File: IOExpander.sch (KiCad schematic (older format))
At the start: 6 parts, among them U11 MCP23017_SO

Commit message: start placement
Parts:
- renumbered C18 to C45, R12 to R75, R13 to R76, R14 to R77, R15 to R78, U11 to U7

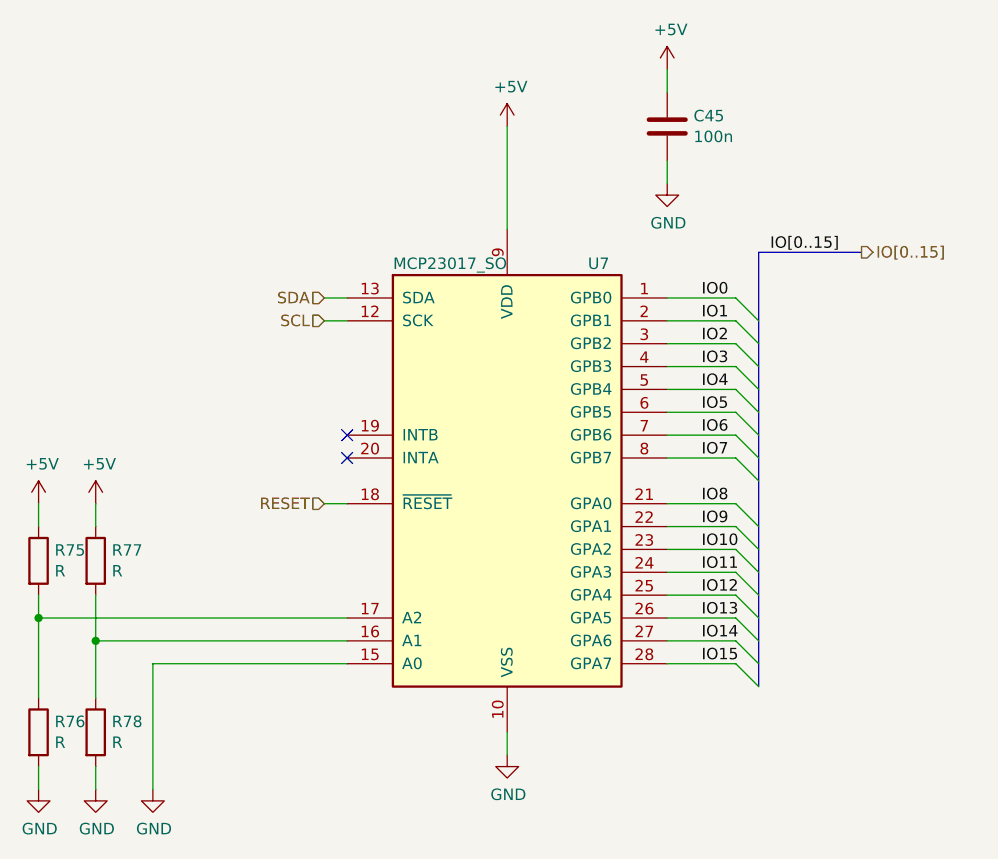
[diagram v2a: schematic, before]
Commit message: add TLE5602
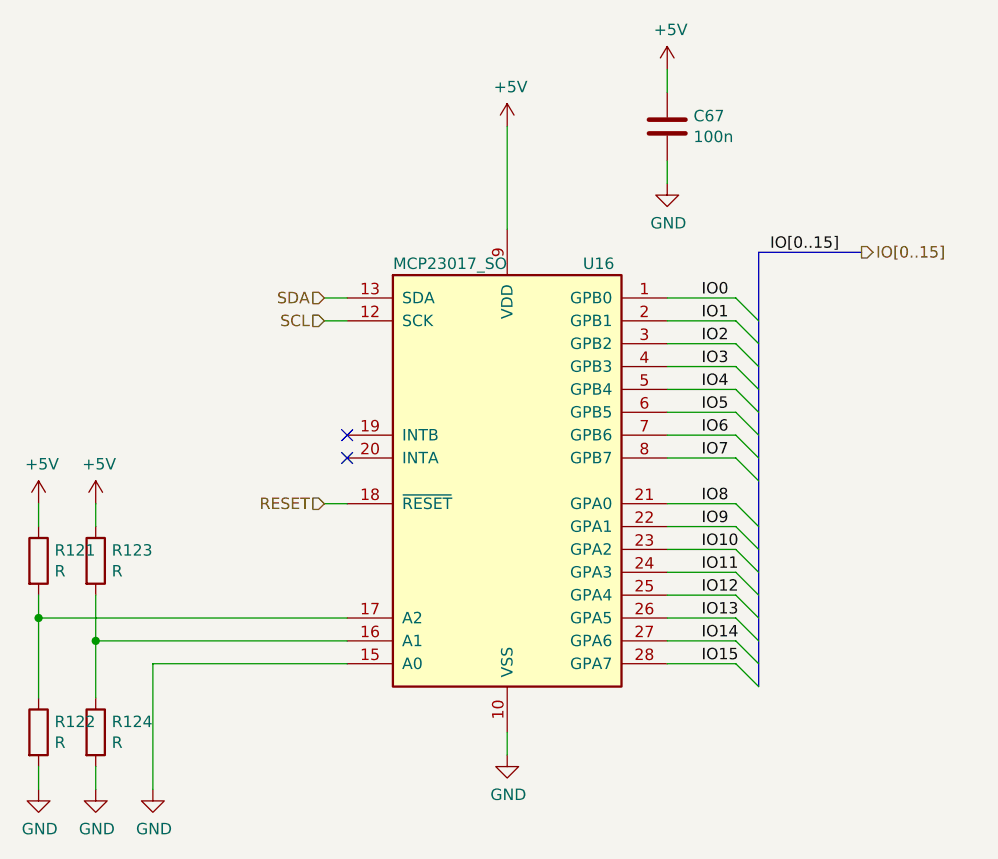
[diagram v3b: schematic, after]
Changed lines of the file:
@@
 $Descr A4 11693 8268
 encoding utf-8
-Sheet 8 22
+Sheet 13 22
 Title ""
 Date ""
@@
 AR Path="/60ADDFFD/60729756" Ref="C?"  Part="1"
 AR Path="/60ADEB0F/60ADF1EF/60729756" Ref="C67"  Part="1"
-F 0 "C45" H 5265 1596 50  0000 L CNN
+F 0 "C67" H 5265 1596 50  0000 L CNN
 F 1 "100n" H 5265 1505 50  0000 L CNN
 F 2 "Capacitor_SMD:C_0603_1608Metric" H 5188 1400 50  0001 C CNN
@@
 AR Path="/60ADDFFD/607B188F" Ref="R?"  Part="1"
 AR Path="/60ADEB0F/60ADF1EF/607B188F" Ref="R124"  Part="1"
-F 0 "R78" H 2720 4246 50  0000 L CNN
+F 0 "R124" H 2720 4246 50  0000 L CNN
 F 1 "R" H 2720 4155 50  0000 L CNN
 F 2 "Resistor_SMD:R_0603_1608Metric" V 2580 4200 50  0001 C CNN
@@
 AR Path="/60ADDFFD/607B24D6" Ref="R?"  Part="1"
 AR Path="/60ADEB0F/60ADF1EF/607B24D6" Ref="R122"  Part="1"
-F 0 "R76" H 2470 4246 50  0000 L CNN
+F 0 "R122" H 2470 4246 50  0000 L CNN
 F 1 "R" H 2470 4155 50  0000 L CNN
 F 2 "Resistor_SMD:R_0603_1608Metric" V 2330 4200 50  0001 C CNN
@@
 AR Path="/60ADDFFD/607B4040" Ref="R?"  Part="1"
 AR Path="/60ADEB0F/60ADF1EF/607B4040" Ref="R123"  Part="1"
-F 0 "R77" H 2720 3496 50  0000 L CNN
+F 0 "R123" H 2720 3496 50  0000 L CNN
 F 1 "R" H 2720 3405 50  0000 L CNN
 F 2 "Resistor_SMD:R_0603_1608Metric" V 2580 3450 50  0001 C CNN
@@
 AR Path="/60ADDFFD/607B4D77" Ref="R?"  Part="1"
 AR Path="/60ADEB0F/60ADF1EF/607B4D77" Ref="R121"  Part="1"
-F 0 "R75" H 2470 3496 50  0000 L CNN
+F 0 "R121" H 2470 3496 50  0000 L CNN
 F 1 "R" H 2470 3405 50  0000 L CNN
 F 2 "Resistor_SMD:R_0603_1608Metric" V 2330 3450 50  0001 C CNN
@@
 AR Path="/60ADDFFD/607270E1" Ref="U?"  Part="1"
 AR Path="/60ADEB0F/60ADF1EF/607270E1" Ref="U16"  Part="1"
-F 0 "U7" H 4850 4050 50  0000 C CNN
+F 0 "U16" H 4850 4050 50  0000 C CNN
 F 1 "MCP23017_SO" H 4200 4050 50  0000 C CNN
 F 2 "Package_SO:SOIC-28W_7.5x17.9mm_P1.27mm" H 4650 2100 50  0001 L CNN

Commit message: placement, routing
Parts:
- removed R75, R76, R77, R78: R, Resistor_SMD:R_0603_1608Metric, symbol AR2ISS:R
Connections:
- net GND: no longer U7.15 (A0)
- net A1: now reaches U7.16 (A1)
- net A2: now reaches U7.17 (A2)
- new net A0: U7.15 (A0)
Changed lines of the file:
@@
 $Descr A4 11693 8268
 encoding utf-8
-Sheet 13 22
+Sheet 7 22
 Title ""
 Date ""
@@
 AR Path="/60ADDFFD/607285C4" Ref="#PWR?"  Part="1"
 AR Path="/60ADEB0F/60ADF1EF/607285C4" Ref="#PWR0180"  Part="1"
-F 0 "#PWR0180" H 4450 4050 50  0001 C CNN
+F 0 "#PWR094" H 4450 4050 50  0001 C CNN
 F 1 "GND" H 4455 4127 50  0000 C CNN
 F 2 "" H 4450 4300 50  0001 C CNN
@@
 AR Path="/60ADDFFD/60728B72" Ref="#PWR?"  Part="1"
 AR Path="/60ADEB0F/60ADF1EF/60728B72" Ref="#PWR0179"  Part="1"
-F 0 "#PWR0179" H 4450 1400 50  0001 C CNN
+F 0 "#PWR093" H 4450 1400 50  0001 C CNN
 F 1 "+5V" H 4465 1723 50  0000 C CNN
 F 2 "" H 4450 1550 50  0001 C CNN
@@
 AR Path="/60ADDFFD/60729756" Ref="C?"  Part="1"
 AR Path="/60ADEB0F/60ADF1EF/60729756" Ref="C67"  Part="1"
-F 0 "C67" H 5265 1596 50  0000 L CNN
+F 0 "C45" H 5265 1596 50  0000 L CNN
 F 1 "100n" H 5265 1505 50  0000 L CNN
 F 2 "Capacitor_SMD:C_0603_1608Metric" H 5188 1400 50  0001 C CNN
@@
 AR Path="/60ADDFFD/60729F21" Ref="#PWR?"  Part="1"
 AR Path="/60ADEB0F/60ADF1EF/60729F21" Ref="#PWR0181"  Part="1"
-F 0 "#PWR0181" H 5150 1150 50  0001 C CNN
+F 0 "#PWR095" H 5150 1150 50  0001 C CNN
 F 1 "+5V" H 5165 1473 50  0000 C CNN
 F 2 "" H 5150 1300 50  0001 C CNN
@@
 AR Path="/60ADDFFD/6072A25B" Ref="#PWR?"  Part="1"
 AR Path="/60ADEB0F/60ADF1EF/6072A25B" Ref="#PWR0182"  Part="1"
-F 0 "#PWR0182" H 5150 1550 50  0001 C CNN
+F 0 "#PWR096" H 5150 1550 50  0001 C CNN
 F 1 "GND" H 5155 1627 50  0000 C CNN
 F 2 "" H 5150 1800 50  0001 C CNN
@@
 Text Label 5600 2100 0    50   ~ 0
 IO[0..15]
-$Comp
-L power:GND #PWR?
-U 1 1 607ACAD8
-P 2900 4450
-AR Path="/607267A8/607ACAD8" Ref="#PWR?"  Part="1"
-AR Path="/60679D69/607ACAD8" Ref="#PWR?"  Part="1"
-AR Path="/60A2B663/607ACAD8" Ref="#PWR092"  Part="1"
-AR Path="/60A2BC9C/607ACAD8" Ref="#PWR0120"  Part="1"
-AR Path="/60ADDFFD/607ACAD8" Ref="#PWR?"  Part="1"
-AR Path="/60ADEB0F/60ADF1EF/607ACAD8" Ref="#PWR0178"  Part="1"
-F 0 "#PWR0178" H 2900 4200 50  0001 C CNN
-F 1 "GND" H 2905 4277 50  0000 C CNN
-F 2 "" H 2900 4450 50  0001 C CNN
-F 3 "" H 2900 4450 50  0001 C CNN
-	1    2900 4450
-	1    0    0    -1
-$EndComp
-$Comp
-L AR2ISS:R R?
-U 1 1 607B188F
-P 2650 4200
-AR Path="/60679D69/607B188F" Ref="R?"  Part="1"
-AR Path="/607267A8/607B188F" Ref="R?"  Part="1"
-AR Path="/60A2B663/607B188F" Ref="R78"  Part="1"
-AR Path="/60A2BC9C/607B188F" Ref="R102"  Part="1"
-AR Path="/60ADDFFD/607B188F" Ref="R?"  Part="1"
-AR Path="/60ADEB0F/60ADF1EF/607B188F" Ref="R124"  Part="1"
-F 0 "R124" H 2720 4246 50  0000 L CNN
-F 1 "R" H 2720 4155 50  0000 L CNN
-F 2 "Resistor_SMD:R_0603_1608Metric" V 2580 4200 50  0001 C CNN
-F 3 "~" H 2650 4200 50  0001 C CNN
-	1    2650 4200
-	1    0    0    -1
-$EndComp
-$Comp
-L power:GND #PWR?
-U 1 1 607B1895
-P 2650 4450
-AR Path="/607267A8/607B1895" Ref="#PWR?"  Part="1"
-AR Path="/60679D69/607B1895" Ref="#PWR?"  Part="1"
-AR Path="/60A2B663/607B1895" Ref="#PWR091"  Part="1"
-AR Path="/60A2BC9C/607B1895" Ref="#PWR0119"  Part="1"
-AR Path="/60ADDFFD/607B1895" Ref="#PWR?"  Part="1"
-AR Path="/60ADEB0F/60ADF1EF/607B1895" Ref="#PWR0177"  Part="1"
-F 0 "#PWR0177" H 2650 4200 50  0001 C CNN
-F 1 "GND" H 2655 4277 50  0000 C CNN
-F 2 "" H 2650 4450 50  0001 C CNN
-F 3 "" H 2650 4450 50  0001 C CNN
-	1    2650 4450
-	1    0    0    -1
-$EndComp
-Wire Wire Line
-	2650 4350 2650 4450
-$Comp
-L AR2ISS:R R?
-U 1 1 607B24D6
-P 2400 4200
-AR Path="/60679D69/607B24D6" Ref="R?"  Part="1"
-AR Path="/607267A8/607B24D6" Ref="R?"  Part="1"
-AR Path="/60A2B663/607B24D6" Ref="R76"  Part="1"
-AR Path="/60A2BC9C/607B24D6" Ref="R100"  Part="1"
-AR Path="/60ADDFFD/607B24D6" Ref="R?"  Part="1"
-AR Path="/60ADEB0F/60ADF1EF/607B24D6" Ref="R122"  Part="1"
-F 0 "R122" H 2470 4246 50  0000 L CNN
-F 1 "R" H 2470 4155 50  0000 L CNN
-F 2 "Resistor_SMD:R_0603_1608Metric" V 2330 4200 50  0001 C CNN
-F 3 "~" H 2400 4200 50  0001 C CNN
-	1    2400 4200
-	1    0    0    -1
-$EndComp
-$Comp
-L power:GND #PWR?
-U 1 1 607B24DC
-P 2400 4450
-AR Path="/607267A8/607B24DC" Ref="#PWR?"  Part="1"
-AR Path="/60679D69/607B24DC" Ref="#PWR?"  Part="1"
-AR Path="/60A2B663/607B24DC" Ref="#PWR089"  Part="1"
-AR Path="/60A2BC9C/607B24DC" Ref="#PWR0117"  Part="1"
-AR Path="/60ADDFFD/607B24DC" Ref="#PWR?"  Part="1"
-AR Path="/60ADEB0F/60ADF1EF/607B24DC" Ref="#PWR0175"  Part="1"
-F 0 "#PWR0175" H 2400 4200 50  0001 C CNN
-F 1 "GND" H 2405 4277 50  0000 C CNN
-F 2 "" H 2400 4450 50  0001 C CNN
-F 3 "" H 2400 4450 50  0001 C CNN
-	1    2400 4450
-	1    0    0    -1
-$EndComp
-Wire Wire Line
-	2400 4350 2400 4450
-$Comp
-L AR2ISS:R R?
-U 1 1 607B4040
-P 2650 3450
-AR Path="/60679D69/607B4040" Ref="R?"  Part="1"
-AR Path="/607267A8/607B4040" Ref="R?"  Part="1"
-AR Path="/60A2B663/607B4040" Ref="R77"  Part="1"
-AR Path="/60A2BC9C/607B4040" Ref="R101"  Part="1"
-AR Path="/60ADDFFD/607B4040" Ref="R?"  Part="1"
-AR Path="/60ADEB0F/60ADF1EF/607B4040" Ref="R123"  Part="1"
-F 0 "R123" H 2720 3496 50  0000 L CNN
-F 1 "R" H 2720 3405 50  0000 L CNN
-F 2 "Resistor_SMD:R_0603_1608Metric" V 2580 3450 50  0001 C CNN
-F 3 "~" H 2650 3450 50  0001 C CNN
-	1    2650 3450
-	1    0    0    -1
-$EndComp
-$Comp
-L power:+5V #PWR?
-U 1 1 607B4046
-P 2650 3200
-AR Path="/607267A8/607B4046" Ref="#PWR?"  Part="1"
-AR Path="/60679D69/607B4046" Ref="#PWR?"  Part="1"
-AR Path="/60A2B663/607B4046" Ref="#PWR090"  Part="1"
-AR Path="/60A2BC9C/607B4046" Ref="#PWR0118"  Part="1"
-AR Path="/60ADDFFD/607B4046" Ref="#PWR?"  Part="1"
-AR Path="/60ADEB0F/60ADF1EF/607B4046" Ref="#PWR0176"  Part="1"
-F 0 "#PWR0176" H 2650 3050 50  0001 C CNN
-F 1 "+5V" H 2665 3373 50  0000 C CNN
-F 2 "" H 2650 3200 50  0001 C CNN
-F 3 "" H 2650 3200 50  0001 C CNN
-	1    2650 3200
-	1    0    0    -1
-$EndComp
-Wire Wire Line
-	2650 3200 2650 3300
-$Comp
-L AR2ISS:R R?
-U 1 1 607B4D77
-P 2400 3450
-AR Path="/60679D69/607B4D77" Ref="R?"  Part="1"
-AR Path="/607267A8/607B4D77" Ref="R?"  Part="1"
-AR Path="/60A2B663/607B4D77" Ref="R75"  Part="1"
-AR Path="/60A2BC9C/607B4D77" Ref="R99"  Part="1"
-AR Path="/60ADDFFD/607B4D77" Ref="R?"  Part="1"
-AR Path="/60ADEB0F/60ADF1EF/607B4D77" Ref="R121"  Part="1"
-F 0 "R121" H 2470 3496 50  0000 L CNN
-F 1 "R" H 2470 3405 50  0000 L CNN
-F 2 "Resistor_SMD:R_0603_1608Metric" V 2330 3450 50  0001 C CNN
-F 3 "~" H 2400 3450 50  0001 C CNN
-	1    2400 3450
-	1    0    0    -1
-$EndComp
-$Comp
-L power:+5V #PWR?
-U 1 1 607B4D7D
-P 2400 3200
-AR Path="/607267A8/607B4D7D" Ref="#PWR?"  Part="1"
-AR Path="/60679D69/607B4D7D" Ref="#PWR?"  Part="1"
-AR Path="/60A2B663/607B4D7D" Ref="#PWR088"  Part="1"
-AR Path="/60A2BC9C/607B4D7D" Ref="#PWR0116"  Part="1"
-AR Path="/60ADDFFD/607B4D7D" Ref="#PWR?"  Part="1"
-AR Path="/60ADEB0F/60ADF1EF/607B4D7D" Ref="#PWR0174"  Part="1"
-F 0 "#PWR0174" H 2400 3050 50  0001 C CNN
-F 1 "+5V" H 2415 3373 50  0000 C CNN
-F 2 "" H 2400 3200 50  0001 C CNN
-F 3 "" H 2400 3200 50  0001 C CNN
-	1    2400 3200
-	1    0    0    -1
-$EndComp
-Wire Wire Line
-	2400 3200 2400 3300
-Wire Wire Line
-	2400 3700 2400 3600
-Wire Wire Line
-	2400 3700 2400 4050
-Connection ~ 2400 3700
-Wire Wire Line
-	2650 3800 2650 3600
-Wire Wire Line
-	2650 4050 2650 3800
-Connection ~ 2650 3800
 NoConn ~ 3750 3000
-Wire Wire Line
-	2900 3900 2900 4450
-Wire Wire Line
-	2400 3700 3750 3700
-Wire Wire Line
-	2650 3800 3750 3800
-Wire Wire Line
-	2900 3900 3750 3900
 Wire Wire Line
 	3650 2300 3750 2300
@@
 AR Path="/60ADDFFD/607270E1" Ref="U?"  Part="1"
 AR Path="/60ADEB0F/60ADF1EF/607270E1" Ref="U16"  Part="1"
-F 0 "U16" H 4850 4050 50  0000 C CNN
+F 0 "U7" H 4850 4050 50  0000 C CNN
 F 1 "MCP23017_SO" H 4200 4050 50  0000 C CNN
 F 2 "Package_SO:SOIC-28W_7.5x17.9mm_P1.27mm" H 4650 2100 50  0001 L CNN
@@
 $EndComp
 NoConn ~ 3750 2900
+Text HLabel 3650 3900 0    50   Input ~ 0
+A0
+Text HLabel 3650 3800 0    50   Input ~ 0
+A1
+Text HLabel 3650 3700 0    50   Input ~ 0
+A2
+Wire Wire Line
+	3650 3700 3750 3700
+Wire Wire Line
+	3750 3800 3650 3800
+Wire Wire Line
+	3650 3900 3750 3900
 Wire Bus Line
 	5550 2100 5550 4000
